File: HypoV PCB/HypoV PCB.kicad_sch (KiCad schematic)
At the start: 7 parts

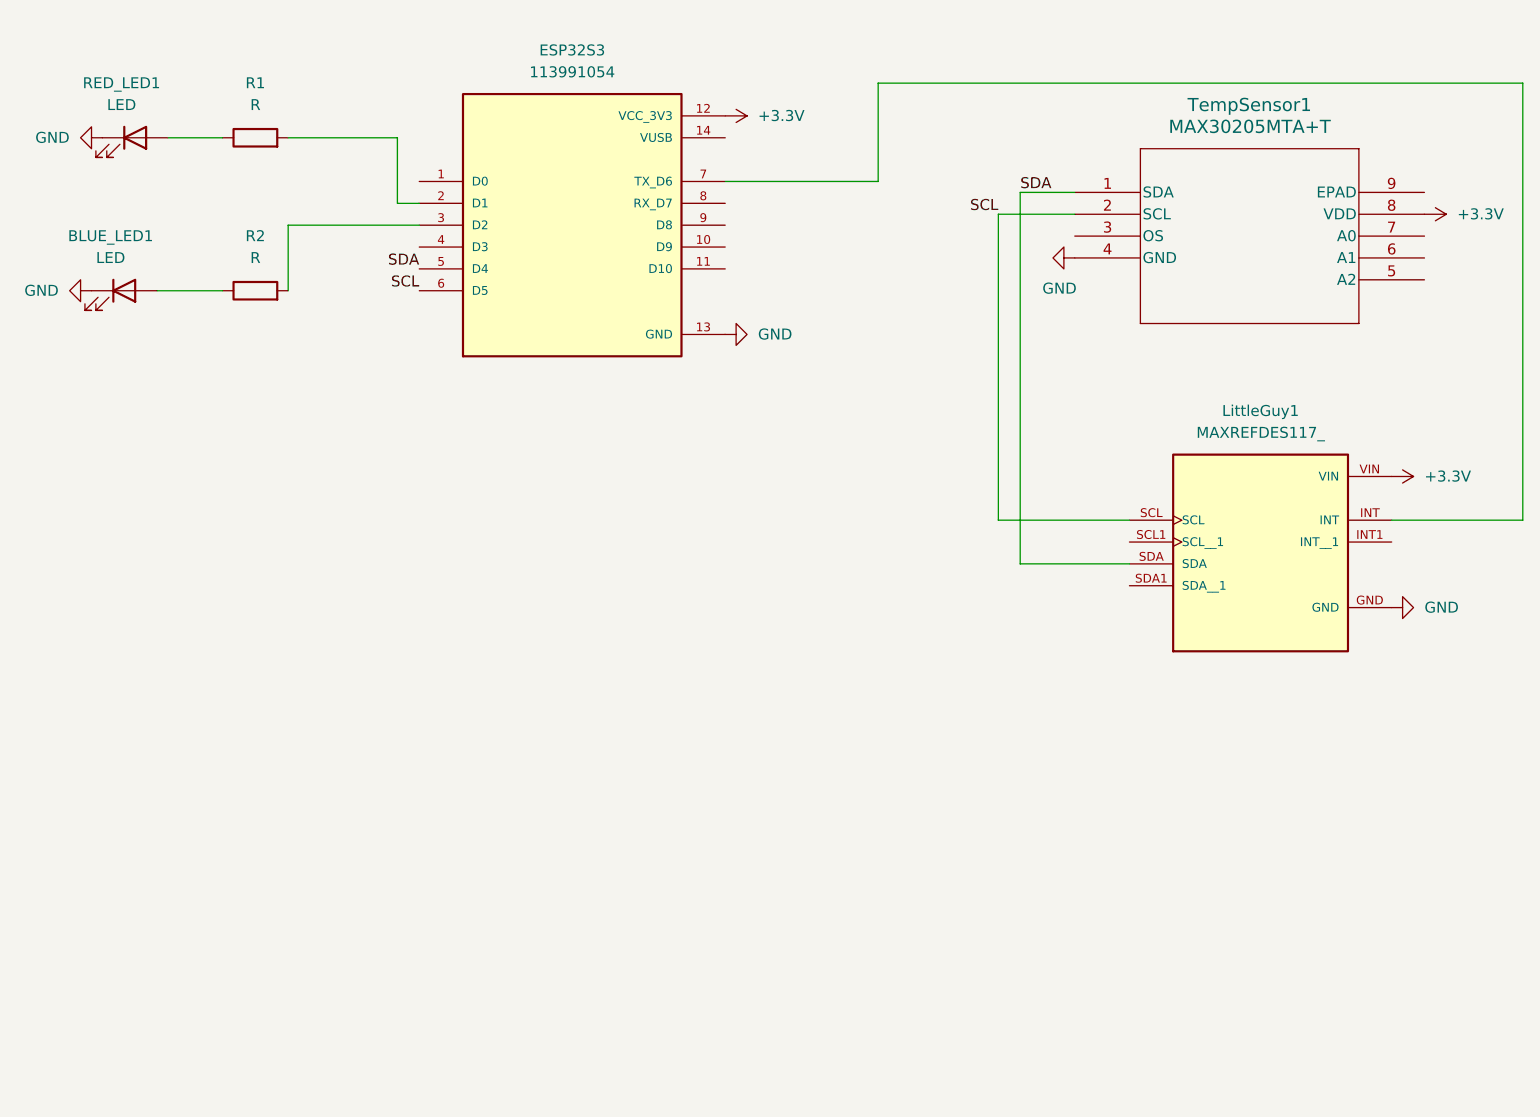
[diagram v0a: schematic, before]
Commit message: started wiring up temp sensor according to datasheet
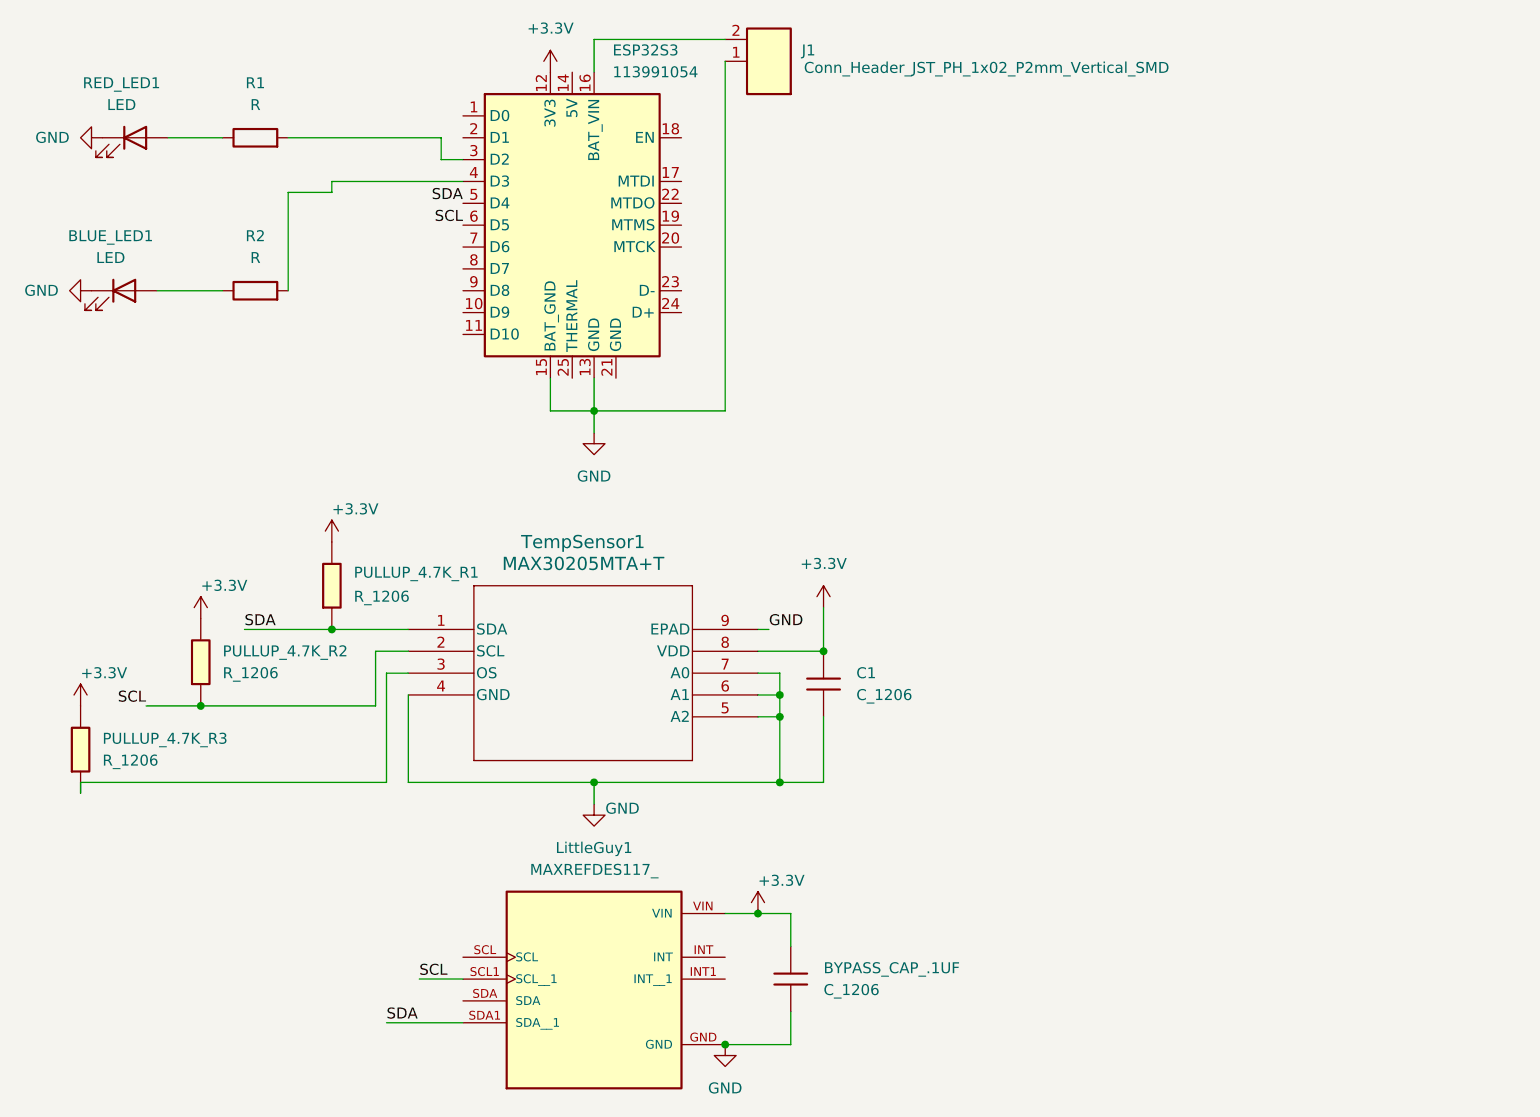
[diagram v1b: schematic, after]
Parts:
- added BYPASS_CAP_.1UF, C1: C_1206, PCM_fab:C_1206, symbol PCM_fab:C_1206
- added J1: Conn_Header_JST_PH_1x02_P2mm_Vertical_SMD, PCM_fab:Header_JST_PH_1x02_P2mm_Vertical_SMD, symbol fab:Conn_Header_JST_PH_1x02_P2mm_Vertical_SMD
- added PULLUP_4.7K_R1, PULLUP_4.7K_R2, PULLUP_4.7K_R3: R_1206, PCM_fab:R_1206, symbol fab:R_1206
- ESP32S3: footprint RF_Module:MCU_Seeed_ESP32C3 -> PCM_fab:SeeedStudio_XIAO_ESP32S3; symbol 113991054:113991054 -> fab:Module_XIAO-ESP32S3
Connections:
- net +3.3V: now also BYPASS_CAP_.1UF.1, C1.1, PULLUP_4.7K_R1.1, PULLUP_4.7K_R2.1, PULLUP_4.7K_R3.1
- net GND: now also ESP32S3.15 (BAT_GND), TempSensor1.5 (A2), TempSensor1.6 (A1), TempSensor1.7 (A0), TempSensor1.9 (EPAD), BYPASS_CAP_.1UF.2, C1.2, J1.1
- net SCL: now also LittleGuy1.SCL1 (SCL__1), PULLUP_4.7K_R2.2; no longer LittleGuy1.SCL
- net SDA: now also LittleGuy1.SDA1 (SDA__1), PULLUP_4.7K_R1.2; no longer LittleGuy1.SDA
- net at LittleGuy1.INT: no longer ESP32S3.7 (TX_D6)
- net at R2.2: now also ESP32S3.4 (D3); no longer ESP32S3.3 (D2)
- net at ESP32S3.2 (D1): no longer R1.2
- net at TempSensor1.3 (OS): now also PULLUP_4.7K_R3.2
- new net: ESP32S3.16 (BAT_VIN), J1.2
- new net: ESP32S3.3 (D2), R1.2
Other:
- moved on the sheet: LittleGuy1, TempSensor1

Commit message: added the breakout board
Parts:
- removed BYPASS_CAP_.1UF: C_1206, PCM_fab:C_1206, symbol PCM_fab:C_1206
- added J2: Conn_01x08_Pin, Connector_PinHeader_2.54mm:PinHeader_1x08_P2.54mm_Vertical, symbol Connector:Conn_01x08_Pin
- R1, R2: footprint Resistor_THT:R_Axial_DIN0207_L6.3mm_D2.5mm_P10.16mm_Horizontal -> PCM_fab:R_1206; symbol Device:R -> fab:R_1206
- renumbered C1 to BYPASS_CAP_.1UF1
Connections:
- net SDA: now also LittleGuy1.SDA
- net D9: now reaches LittleGuy1.INT
- net D9: now also ESP32S3.10 (D9)
- net at R2.2: now also ESP32S3.9 (D8); no longer ESP32S3.4 (D3)
- net at ESP32S3.3 (D2): no longer R1.2
- net OS: now reaches ESP32S3.7 (D6)
- net OS: now also PULLUP_4.7K_R3.2, TempSensor1.3 (OS)
- net at ESP32S3.8 (D7): now also R1.2
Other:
- moved on the sheet: PULLUP_4.7K_R1, PULLUP_4.7K_R3
